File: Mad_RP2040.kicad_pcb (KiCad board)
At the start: 2 copper layers, 60.1 x 69.1 mm, 79 parts, among them J1 USB_C_Receptacle, J2 Conn_ARM_SWD_TagConnect_TC203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, Q1 2N7002VC-7, SW1 PEC11R, SW10 TL3780AF240QG, SW2 SW_SPST, SW3 SW_SPST, SW4 PEC11R, SW5 SW_SPST, SW6 SW_SPST, SW7 PEC11R, SW8 SW_SPST, SW9 SW_SPST, U0 PCB, U1 ECMF02-2AMX6, U3 NCP1117-3.3_SOT223, U4 GD25Q127CWIGR, U5 RP2040, X1 ECS-2520MVLC-120-CN

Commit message: Board update
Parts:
- removed the C10 at (134.2, 77.8)
- removed the C11 at (85.6, 46.4)
- removed C26, C27: 100nF, Capacitor_SMD:C_0402_1005Metric
- removed the C6 at (82.4, 45.0)
- removed the C7 at (80.8, 49.2)
- removed the C8 at (85.6, 40.5)
- removed the C9 at (85.6, 42.5)
- removed D10, D11, D15, D16: SK6812_MINI_E, Mad_Footprints:SK6812_MINI_E
- removed D12, D13, D14, D17, D3, D4, D8, D9: LL4148, Diode_SMD:D_MiniMELF
- removed the D5 at (85.4, 72.9)
- removed the D6 at (130.5, 105.5)
- removed the D7 at (130.5, 125.0)
- removed R3, R5: 2K2, Resistor_SMD:R_0402_1005Metric
- removed R4: 5K1, Resistor_SMD:R_0402_1005Metric
- removed the SW3 at (111.0, 130.5)
- removed SW4, SW7: PEC11R, Mad_Footprints:RotaryEncoder_Bourns_Vertical_PEC12R-3x17F-Sxxxx
- removed SW5, SW6, SW8, SW9: SW_SPST, Mad_Footprints:SW_Hotswap_Kailh_MX_1.00u
- added C19: 100nF, Capacitor_SMD:C_0402_1005Metric, F.Cu at (148.3, 80.2)
- added C20: 100nF, Capacitor_SMD:C_0402_1005Metric, B.Cu at (154.8, 80.6)
- added C21: 100nF, Capacitor_SMD:C_0402_1005Metric, B.Cu at (144.2, 79.2)
- C12: renamed from C19; moved to F.Cu
- C4, C5, U3: moved to F.Cu
- D5: renamed from D1; value SK6812_MINI_E -> WS2812B-2020
- D6: renamed from D2; value LED -> GREEN
- SW1: value PEC11R -> SW_SPST; footprint Mad_Footprints:RotaryEncoder_Bourns_Vertical_PEC12R-3x17F-Sxxxx -> Mad_Footprints:SW_Hotswap_Kailh_MX_1.00u
- moved SW3 69.8 mm to (158.0, 73.4)
- moved R12 60.3 mm to (158.1, 65.7)
- moved R9 60.3 mm to (159.7, 67.8)
- moved C8 60.3 mm to (156.3, 66.2)
- moved C9 60.3 mm to (147.3, 67.0)
- moved D7 60.3 mm to (152.1, 67.1)
- moved Q1 60.3 mm to (152.3, 63.4)
- moved R11 60.3 mm to (154.8, 65.7)
- moved R6 60.3 mm to (151.7, 65.3)
- moved R8 60.3 mm to (144.9, 66.8)
- moved R7 60.3 mm to (144.9, 64.8)
- moved C6 56.4 mm to (134.9, 61.9)
- moved SW2 42.9 mm to (150.5, 94.2), turned to 90 degrees
- moved D6 31.2 mm to (141.5, 62.2)
- moved J2 24.2 mm to (158.3, 83.7), turned to 90 degrees
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- renumbered C17 to C10, C18 to C11, C20 to C13, C21 to C14, C22 to C15, C23 to C16, C24 to C17, C25 to C18, C12 to C6, C13 to C7, C15 to C8, C16 to C9, D18 to D7, SW10 to SW3, U0 to U2
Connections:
- net /RP2040a/A0 renamed /RP2040/A0
- net /RP2040a/A1 renamed /RP2040/A1
- net /RP2040a/A2 renamed /RP2040/A2
- net /RP2040a/A3 renamed /RP2040/A3
- net /RP2040a/IO_10 renamed /RP2040/IO_10
- net /RP2040a/MISO renamed /RP2040/MISO
- net /RP2040a/MOSI renamed /RP2040/MOSI
- net /RP2040a/RP2040/1V1 renamed /RP2040/RP2040/1V1
- net /RP2040a/RP2040/GPIO17 renamed /RP2040/RP2040/GPIO17
- net /RP2040a/RP2040/GPIO18 renamed /RP2040/RP2040/GPIO18
- net /RP2040a/RP2040/GPIO24 renamed /RP2040/RP2040/GPIO24
- net /RP2040a/RP2040/QSPI_SCLK renamed /RP2040/RP2040/QSPI_SCLK
- net /RP2040a/RP2040/QSPI_SD0 renamed /RP2040/RP2040/QSPI_SD0
- net /RP2040a/RP2040/QSPI_SD1 renamed /RP2040/RP2040/QSPI_SD1
- net /RP2040a/RP2040/QSPI_SD2 renamed /RP2040/RP2040/QSPI_SD2
- net /RP2040a/RP2040/QSPI_SD3 renamed /RP2040/RP2040/QSPI_SD3
- net /RP2040a/RP2040/QSPI_~{CS} renamed /RP2040/RP2040/QSPI_~{CS}
- net /RP2040a/RP2040/XTAL_IN renamed /RP2040/RP2040/XTAL_IN
- net /RP2040a/RX0 renamed /RP2040/RX0
- net /RP2040a/SCK renamed /RP2040/SCK
- net /RP2040a/SCL1 renamed /RP2040/SCL1
- net /RP2040a/SDA1 renamed /RP2040/SDA1
- net /RP2040a/STATUS_LED_DO renamed /RP2040/STATUS_LED_DO
- net /RP2040a/SWCLK renamed /RP2040/SWCLK
- net /RP2040a/SWDIO renamed /RP2040/SWDIO
- net /RP2040a/USB_D+ renamed /RP2040/USB_D+
- net /RP2040a/USB_D- renamed /RP2040/USB_D-
- net /RP2040a/~{CS} renamed /RP2040/~{CS}
- net /RP2040a/~{RST} renamed /RP2040/~{RST}
- C10 pad 1: /RP2040a/3V3 -> /RP2040/3V3
- C11 pad 1: /RP2040a/3V3 -> /RP2040/3V3
- C12 pad 1: /RP2040a/3V3 -> /RP2040/3V3
- C14 pad 1: /RP2040a/3V3 -> /RP2040/3V3
- C15 pad 2: /RP2040a/3V3 -> /RP2040/3V3
- C16 pad 1: /RP2040a/3V3 -> /RP2040/3V3
- C17 pad 1: /RP2040a/3V3 -> /RP2040/3V3
- C18 pad 1: /RP2040a/3V3 -> /RP2040/3V3
- C5 pad 1: /RP2040a/3V3 -> /RP2040/3V3
- C6 pad 1: /RP2040a/3V3 -> /RP2040/3V3
- C7 pad 1: /RP2040a/3V3 -> /RP2040/3V3
- D5 pad 1: unconnected-(D1-DOUT-Pad1) -> /RP2040/LED_DO
- D5 pad 4: /RP2040a/3V3 -> /RP2040/3V3
- D6 pad 1: GND -> /RP2040/3V3
- J2 pad 1: /RP2040a/3V3 -> /RP2040/3V3
- R11 pad 2: /RP2040a/3V3 -> /RP2040/3V3
- R7 pad 2: /RP2040a/3V3 -> /RP2040/3V3
- SW2 pad 2: /RP2040a/IO_7 -> /Col0
- SW3 pad 2: /RP2040a/3V3 -> /RP2040/3V3
- U3 pad 2: /RP2040a/3V3 -> /RP2040/3V3
- U4 pad 8: /RP2040a/3V3 -> /RP2040/3V3
- U5 pad 1: /RP2040a/3V3 -> /RP2040/3V3
- U5 pad 10: /RP2040a/3V3 -> /RP2040/3V3
- U5 pad 11: /RP2040a/IO_8 -> /RP2040/IO_8
- U5 pad 12: /RP2040a/IO_9 -> /RP2040/IO_9
- U5 pad 14: /RP2040a/ENC1A -> /RP2040/ENC1A
- U5 pad 15: /RP2040a/ENC1B -> /RP2040/ENC1B
- U5 pad 16: /RP2040a/ENC2A -> /RP2040/ENC2A
- U5 pad 17: /RP2040a/ENC2B -> /RP2040/ENC2B
- U5 pad 18: /RP2040a/ENC3A -> /RP2040/ENC3A
- U5 pad 2: /RP2040a/TX0 -> /TX0
- U5 pad 22: /RP2040a/3V3 -> /RP2040/3V3
- U5 pad 27: /RP2040a/ENC3B -> /RP2040/ENC3B
- U5 pad 30: /RP2040a/VBUS_DETECT -> /RP2040/VBUS_DETECT
- U5 pad 33: /RP2040a/3V3 -> /RP2040/3V3
- U5 pad 42: /RP2040a/3V3 -> /RP2040/3V3
- U5 pad 43: /RP2040a/3V3 -> /RP2040/3V3
- U5 pad 44: /RP2040a/3V3 -> /RP2040/3V3
- U5 pad 48: /RP2040a/3V3 -> /RP2040/3V3
- U5 pad 49: /RP2040a/3V3 -> /RP2040/3V3
- U5 pad 6: /RP2040a/IO_4 -> /Row0
- U5 pad 7: /RP2040a/IO_5 -> /Row1
- U5 pad 8: /RP2040a/IO_6 -> /RP2040/IO_6
- U5 pad 9: /RP2040a/IO_7 -> /Col0
- X1 pad 1: /RP2040a/3V3 -> /RP2040/3V3
- X1 pad 4: /RP2040a/3V3 -> /RP2040/3V3
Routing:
- net /RP2040/3V3: track 0.00 -> 8.19 mm
- net /RP2040a/3V3: track 3.18 -> 0.00 mm
- net /RP2040/RP2040/1V1: track 0.00 -> 1.54 mm
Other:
- board size 60.1 x 69.1 mm -> 38 x 32.1 mm

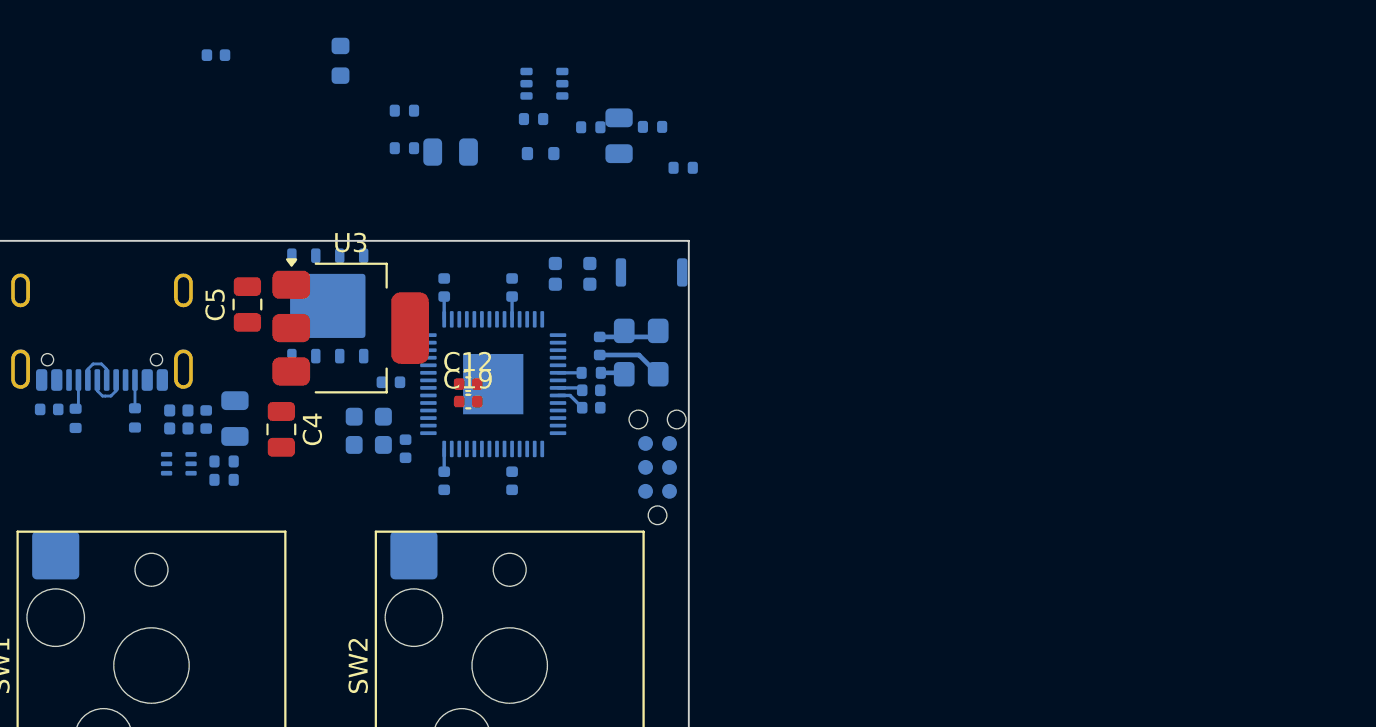
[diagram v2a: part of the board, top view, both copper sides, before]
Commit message: Update github actions
Remove double up on actions

Remove kibot config file to what the action is looking for

Update date on title block

Update github actions

update github action

update schematic

Add options.yaml
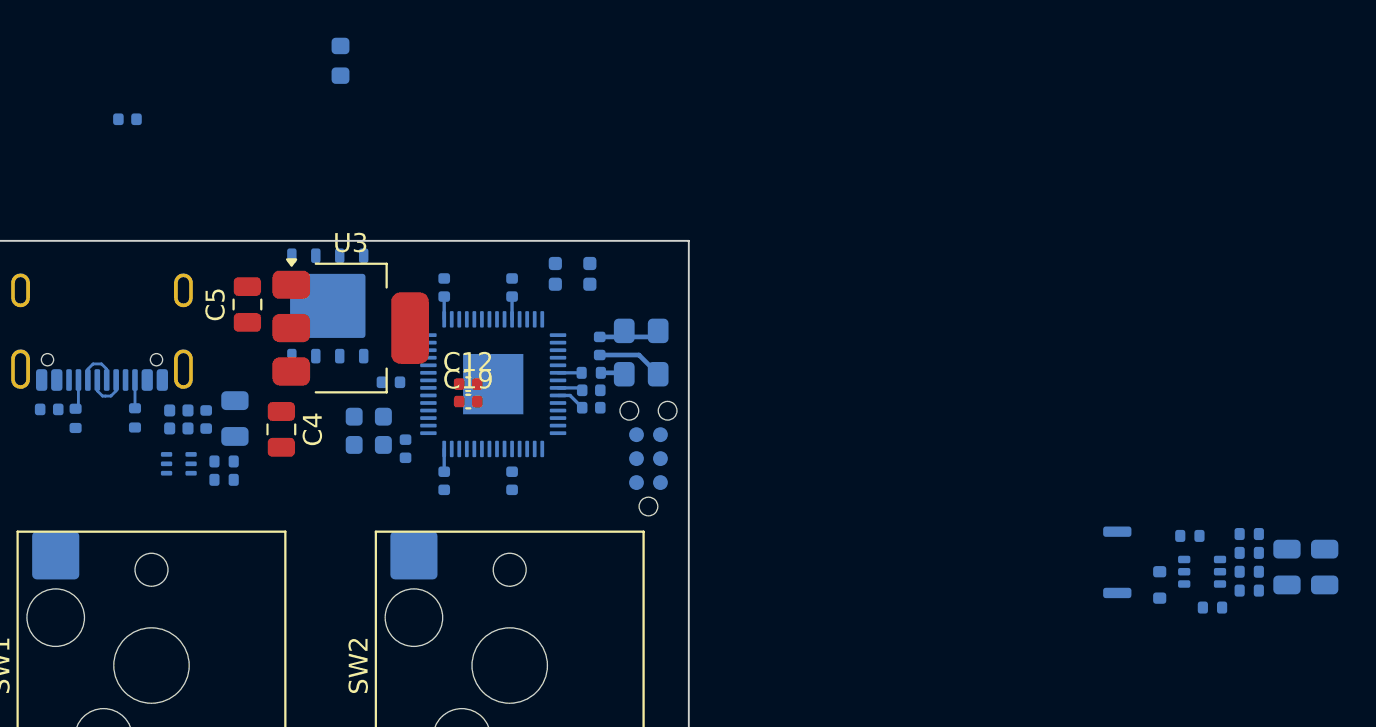
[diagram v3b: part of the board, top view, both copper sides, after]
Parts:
- moved R7 51.5 mm to (189.7, 90.3), turned to 0 degrees
- moved R8 50.1 mm to (189.7, 89.3), turned to 0 degrees
- moved C9 49.5 mm to (191.7, 89.0), turned to -90 degrees
- moved C8 43.9 mm to (193.7, 89.0), turned to -90 degrees
- moved Q1 43.4 mm to (187.2, 89.3)
- moved R6 41.2 mm to (186.6, 87.4)
- moved R11 41.1 mm to (189.7, 87.3)
- moved D7 40.0 mm to (184.9, 90.0), turned to 90 degrees
- moved R12 38.9 mm to (189.7, 88.3), turned to 0 degrees
- moved R9 36.5 mm to (187.8, 91.2)
- moved SW3 29.1 mm to (182.7, 88.8), turned to 90 degrees
- moved C6 5.80 mm to (130.2, 65.3)
- moved J2 0.67 mm to (157.8, 83.3)

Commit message: Finish off part placement
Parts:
- added D1: LL4148, Diode_SMD:D_MiniMELF, B.Cu at (135.6, 101.5)
- added D2: LL4148, Diode_SMD:D_MiniMELF, B.Cu at (154.3, 101.3)
- added D3: SK6812_MINI_E, Mad_Footprints:SK6812_mini_e, B.Cu at (136.9, 94.2)
- added D4: SK6812_MINI_E, Mad_Footprints:SK6812_mini_e, B.Cu at (156.0, 94.2)
- added R3: 5K1, Resistor_SMD:R_0402_1005Metric, B.Cu at (149.2, 86.3)
- added R4: 5K1, Resistor_SMD:R_0402_1005Metric, B.Cu at (149.0, 85.7)
- added R5: 1K, Resistor_SMD:R_0402_1005Metric, B.Cu at (135.9, 73.8)
- C12, C19, C4, C5, U3: moved to B.Cu
- moved U2 75.1 mm to (122.0, 103.5)
- moved C8 39.7 mm to (154.1, 86.6), turned to 180 degrees
- moved C9 37.9 mm to (154.1, 84.6), turned to 180 degrees
- moved R7 34.4 mm to (155.3, 88.5), turned to -90 degrees
- moved R8 32.5 mm to (157.2, 88.5), turned to -90 degrees
- moved R9 31.6 mm to (156.3, 88.5), turned to 90 degrees
- moved R12 31.5 mm to (158.2, 88.5), turned to -90 degrees
- moved R11 30.5 mm to (159.2, 88.5), turned to 90 degrees
- moved Q1 30.1 mm to (157.2, 86.0), turned to -90 degrees
- moved D7 28.3 mm to (157.4, 83.7), turned to 0 degrees
- moved R6 27.5 mm to (159.2, 85.4), turned to -90 degrees
- moved SW3 26.1 mm to (157.6, 81.8), turned to 0 degrees
- moved C5 14.3 mm to (139.9, 89.0), turned to 0 degrees
- moved C6 12.0 mm to (139.9, 72.3), turned to 0 degrees
- moved D6 11.7 mm to (135.9, 72.5), turned to 180 degrees
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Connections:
- D6 pad 1: /RP2040/3V3 -> GND
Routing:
- net /RP2040/RP2040/QSPI_SD3: track 0.00 -> 12.5 mm
- net /RP2040/RP2040/QSPI_SCLK: track 0.00 -> 10.3 mm
- net /RP2040/RP2040/QSPI_SD0: track 0.00 -> 7.47 mm
- net /RP2040/3V3: track 8.19 -> 13.5 mm
- net /RP2040/RP2040/QSPI_~{CS}: track 0.00 -> 4.63 mm
- net /RP2040/RP2040/QSPI_SD1: track 0.00 -> 3.72 mm
- net /RP2040/RP2040/1V1: track 1.54 -> 4.57 mm
- net /RP2040/RP2040/QSPI_SD2: track 0.00 -> 2.89 mm
- net Net-(U1-D+_in): track 2.38 -> 5.07 mm
- net Net-(U1-D-_in): track 2.38 -> 4.03 mm
- added copper zone on B.Cu, net /PreFIlterGND
- added copper zone on F.Cu, net /PreFIlterGND
- added copper zone on B.Cu, net GND
- added copper zone on F.Cu, net GND

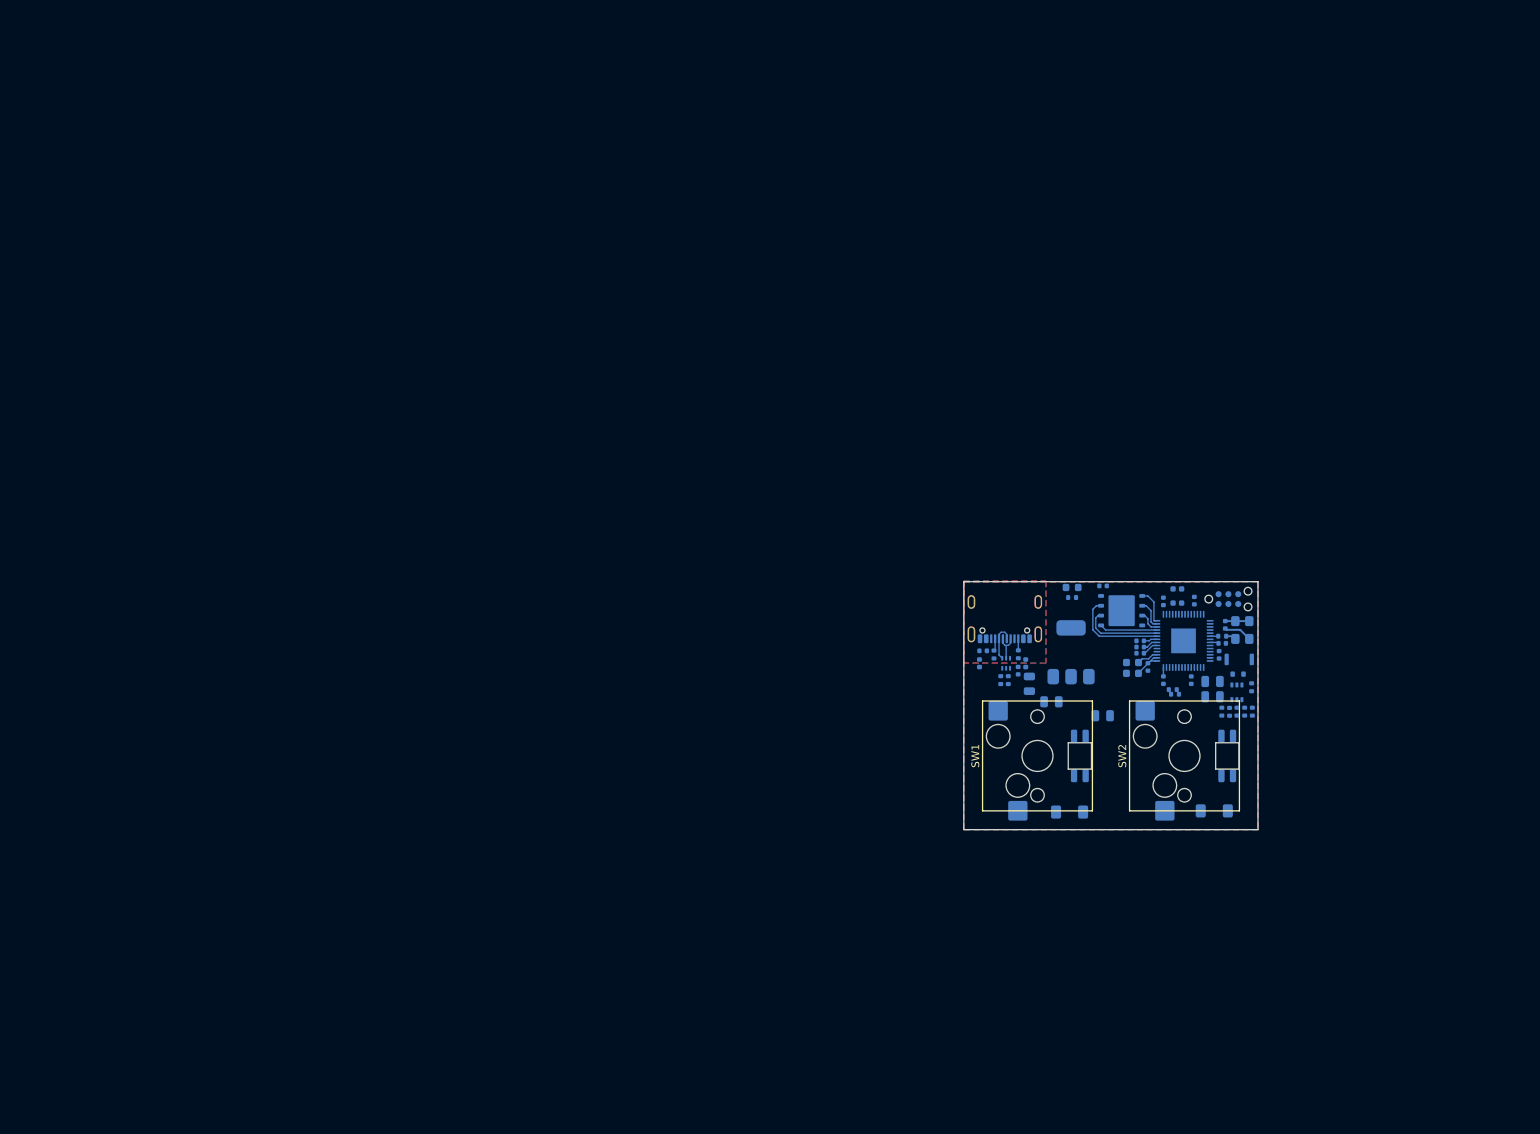
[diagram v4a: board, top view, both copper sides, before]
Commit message: Update Models, Finalize LED selections, add backlight, ...
 add mounting holes, add fids, cleanup
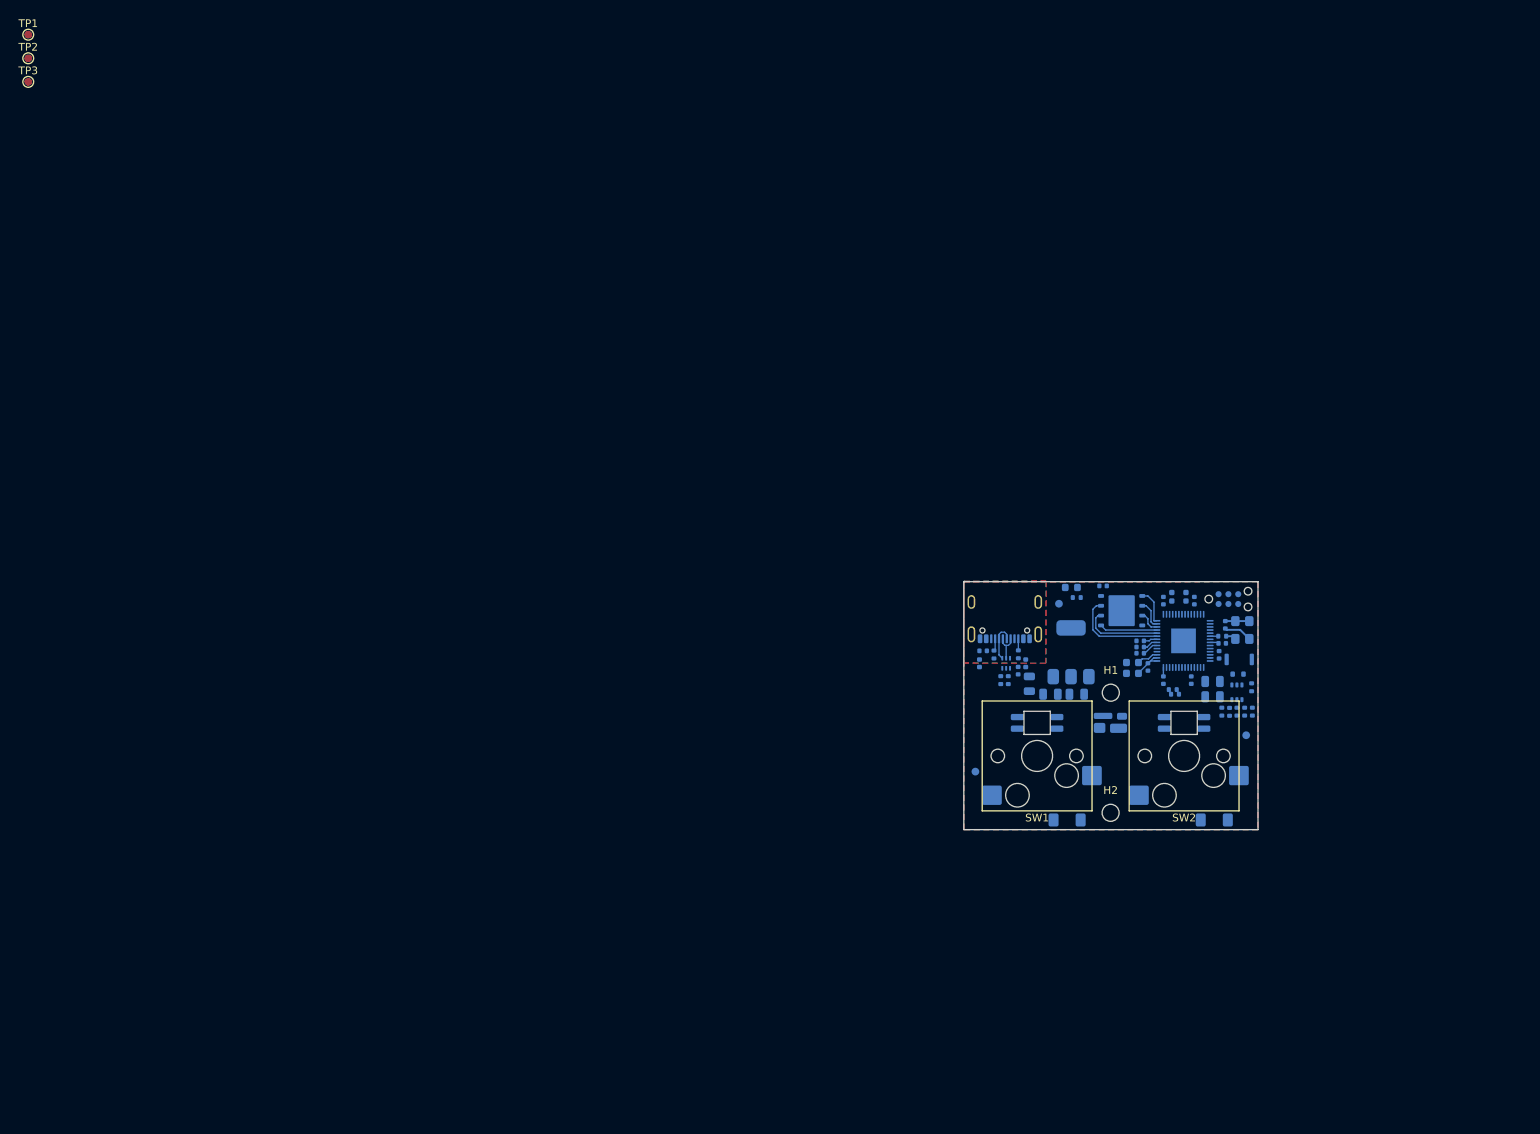
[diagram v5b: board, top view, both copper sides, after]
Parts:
- added D8: SK6812MINI-012, Mad_Footprints:SK6812MINI-012, B.Cu at (140.9, 90.0)
- added FID1: Fiducial, Fiducial:Fiducial_1mm_Mask2mm, B.Cu at (158.4, 91.6)
- added FID2: Fiducial, Fiducial:Fiducial_1mm_Mask2mm, B.Cu at (134.2, 74.6)
- added FID3: Fiducial, Fiducial:Fiducial_1mm_Mask2mm, B.Cu at (123.5, 96.3)
- added H1: MountingHole_Pad, MountingHole:MountingHole_2.2mm_M2_DIN965, F.Cu at (140.9, 86.1)
- added H2: MountingHole_Pad, MountingHole:MountingHole_2.2mm_M2_DIN965, F.Cu at (140.9, 101.6)
- added TP1: Reset, TestPoint:TestPoint_Pad_D1.0mm, F.Cu at (1.02, 1.02)
- added TP2: Delay, TestPoint:TestPoint_Pad_D1.0mm, F.Cu at (1.02, 4.08)
- added TP3: Boot, TestPoint:TestPoint_Pad_D1.0mm, F.Cu at (1.02, 7.12)
- D3, D4: footprint Mad_Footprints:SK6812_mini_e -> Mad_Footprints:SK6812MINI-E
- U1: footprint Package_DFN_QFN:ST_UQFN-6L_1.5x1.7mm_P0.5mm -> Mad_Footprints:ST_UQFN-6L_1.5x1.7mm_P0.5mm
- moved D4 7.03 mm to (150.4, 90.0), turned to 180 degrees
- moved D3 6.99 mm to (131.4, 90.0), turned to 180 degrees
- moved C5 4.35 mm to (136.6, 86.3)
- moved D2 1.18 mm to (154.3, 102.5)
- moved D1 1.08 mm to (135.3, 102.5)
- moved C4 0.98 mm to (133.2, 86.3)
- moved R5 0.60 mm to (136.6, 73.8)
- moved D5 0.22 mm to (149.8, 73.7), turned to 0 degrees
- moved C10 0.10 mm to (147.8, 74.2)
- moved D6 0.10 mm to (135.8, 72.5)
- turned SW1 to 180 degrees
- turned SW2 to 180 degrees
- renumbered U2 to U0
